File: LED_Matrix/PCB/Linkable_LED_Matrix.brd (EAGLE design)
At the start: 32 x 32 mm, 9 parts

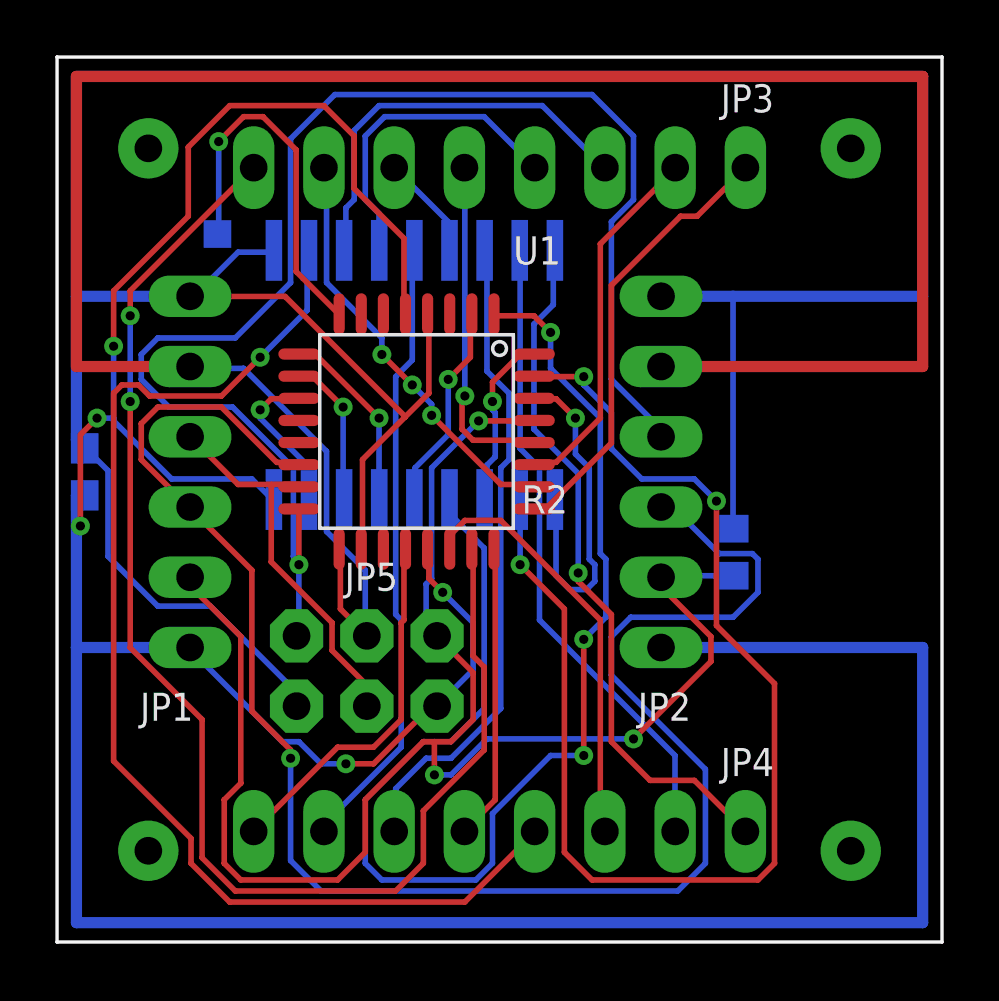
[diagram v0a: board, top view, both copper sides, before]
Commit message: led - matrix - new mounting holes, rerouted...
Added new mounting hole strategy - holes are 0.125" unplated, and can mount
with m2.5 screws, or plastic pressfit standoffs.

Silikscreen cleaned up - all labels moved away from vias, and placed upright.
Added clear labelling for all parts, and put horizontal lines across the board
showing chaining connectivity.

Put ATTINY's decoupling cap closer to part.

12 mil traces for passthru VCC/GND/SCLK.  All others 8mil.

Removed unused test pad.
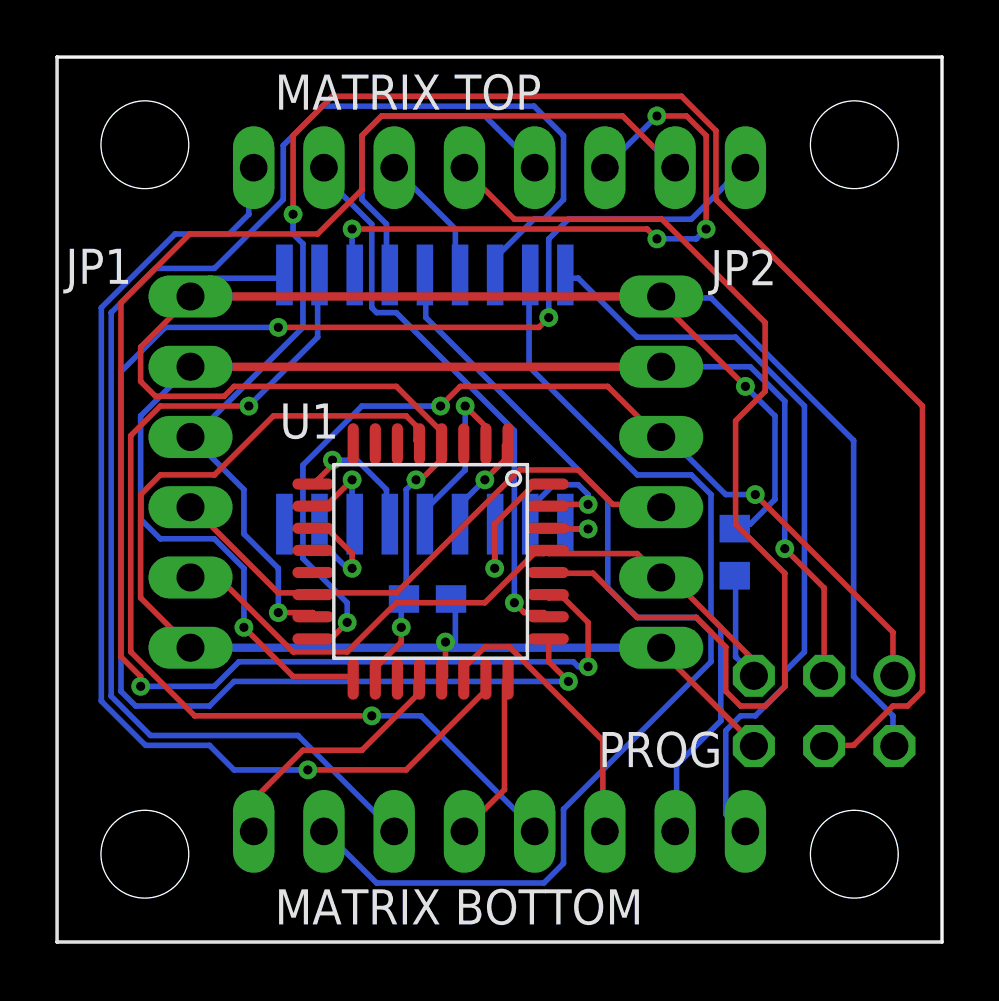
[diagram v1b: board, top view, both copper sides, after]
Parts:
- removed U$1: ATTINY48, ScottSilver:ATTINY48
- removed U$2: ULN2803AFWG, ScottSilver:ULN2803AFWG
- removed U$3: 8X8_LED_MATRIX, ScottSilver:8X8_LED_MATRIX
- removed U$5: 1X1MM_PAD, ScottSilver:1X1MM_PAD
- removed U$6, U$7: DIP1X6MALE, ScottSilver:DIP1X6MALE
- removed U$9: DIP2X3MALE, ScottSilver:DIP2X3MALE
- added JP1, JP2: (no value), raspberrystem:1X06
- added LEDMATRIX: 8X8_LED_MATRIX, raspberrystem:8X8_LED_MATRIX
- added PROG: (no value), raspberrystem:MA03-2
- added U1: ATTINY48, raspberrystem:ATTINY48
- added U2: ULN2803AFWG, raspberrystem:ULN2803AFWG
- moved C1 13.2 mm to (13.4, 12.4), turned to 180 degrees
- moved R1 0.05 mm to (24.5, 14.1)
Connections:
- removed net N$13: U$1.PB7, U$5.P$1
- net COL0: now also U1.PD0, U2.I1; no longer U$1.PD0, U$2.I1
- net COL1: now also U1.PD1, U2.I2; no longer U$1.PD1, U$2.I2
- net COL2: now also U1.PD2, U2.I3; no longer U$1.PD2, U$2.I3
- net COL3: now also U1.PD3, U2.I4; no longer U$1.PD3, U$2.I4
- net COL4: now also U1.PD4, U2.I5; no longer U$1.PD4, U$2.I5
- net COL5: now also U1.PD5, U2.I6; no longer U$1.PD5, U$2.I6
- net COL6: now also U1.PD6, U2.I7; no longer U$1.PD6, U$2.I7
- net COL7: now also U1.PD7, U2.I8; no longer U$1.PD7, U$2.I8
- net CS: now also JP1.4, JP2.4, U1.PB2; no longer U$1.PB2, U$6.3, U$7.3
- net GND: now also JP1.6, JP2.6, PROG.6, U1.AGND, U1.GND; no longer U$1.AGND, U$1.GND, U$2.GND, U$6.1, U$7.1, U$9.GND
- net MISO: now also JP2.3, PROG.1, U1.PB4; no longer U$1.PB4, U$7.4, U$9.MISO
- net MOSI: now also JP1.3, PROG.4, U1.PB3; no longer U$1.PB3, U$6.4, U$9.MOSI
- net N$1: now also LEDMATRIX.COL0, U2.O1; no longer U$2.O1, U$3.COL0
- net N$2: now also LEDMATRIX.COL1, U2.O2; no longer U$2.O2, U$3.COL1
- net N$3: now also LEDMATRIX.COL2, U2.O3; no longer U$2.O3, U$3.COL2
- net N$4: now also LEDMATRIX.COL3, U2.O4; no longer U$2.O4, U$3.COL3
- net N$5: now also LEDMATRIX.COL4, U2.O5; no longer U$2.O5, U$3.COL4
- net N$6: now also LEDMATRIX.COL5, U2.O6; no longer U$2.O6, U$3.COL5
- net N$7: now also LEDMATRIX.COL6, U2.O7; no longer U$2.O7, U$3.COL6
- net N$8: now also LEDMATRIX.COL7, U2.O8; no longer U$2.O8, U$3.COL7
- net RESET: now also JP1.5, JP2.5, PROG.5, U1.PC6; no longer U$1.PC6, U$6.2, U$7.2, U$9.RESET
- net ROW0: now also LEDMATRIX.ROW0, U1.PC7; no longer U$1.PC7, U$3.ROW0
- net ROW1: now also LEDMATRIX.ROW1, U1.PA1; no longer U$1.PA1, U$3.ROW1
- net ROW2: now also LEDMATRIX.ROW2, U1.PC0; no longer U$1.PC0, U$3.ROW2
- net ROW3: now also LEDMATRIX.ROW3, U1.PC1; no longer U$1.PC1, U$3.ROW3
- net ROW4: now also LEDMATRIX.ROW4, U1.PC2; no longer U$1.PC2, U$3.ROW4
- net ROW5: now also LEDMATRIX.ROW5, U1.PC3; no longer U$1.PC3, U$3.ROW5
- net ROW6: now also LEDMATRIX.ROW6, U1.PC4; no longer U$1.PC4, U$3.ROW6
- net ROW7: now also LEDMATRIX.ROW7, U1.PC5; no longer U$1.PC5, U$3.ROW7
- net SCK: now also JP1.2, JP2.2, PROG.3, U1.PB5; no longer U$1.PB5, U$6.5, U$7.5, U$9.SCK
- net VCC: now also JP1.1, JP2.1, PROG.2, U1.AVCC, U1.VCC, U2.COMMON; no longer U$1.AVCC, U$1.VCC, U$2.COMMON, U$6.6, U$7.6, U$9.5V
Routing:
- net GND: track 125.5 -> 43.7 mm, vias 5 -> 1
- net MOSI: track 14.2 -> 66.0 mm, vias 0 -> 2
- net ROW6: track 13.3 -> 59.0 mm, vias 0 -> 2
- net COL3: track 45.9 -> 3.66 mm, vias 3 -> 1
- net ROW4: track 16.1 -> 57.4 mm, vias 0 -> 3
- net CS: track 61.9 -> 20.7 mm, vias 1 -> 0
- net COL1: track 45.0 -> 5.09 mm, vias 3 -> 1
- net VCC: track 110.5 -> 78.5 mm, vias 0 -> 3
- net SCK: track 82.2 -> 50.1 mm, vias 0 -> 2
- net N$3: track 23.6 -> 53.5 mm
- net RESET: track 57.8 -> 29.1 mm, vias 3 -> 0
- net ROW7: track 12.3 -> 39.3 mm, vias 1 -> 0
- net MISO: track 53.3 -> 35.6 mm, vias 1 -> 3
- net N$5: track 22.6 -> 38.7 mm
- net N$13: track 13.6 -> 0.00 mm, vias 1 -> 0
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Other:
- outline, holes or cut-outs redrawn
- board text added: "DOUT"
- board text added: "MATRIX BOTTOM"
- board text added: "MATRIX TOP"
- board text removed: "D_O"
- board text removed: "JP1"
- board text removed: "JP2"
- board text removed: "JP3"
- board text removed: "JP4"
- board text removed: "JP5"
- board text removed: "R1"
- board text removed: "R2"
- board text removed: "U1"
- board text removed: "U2"

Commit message: cleanup to pass error checks
Stop mask fails checks for silkscreen written on top of copper, but OshPark
automatically trims that so I've approved it all.  It would be a pain to trim
it all, so I won't (unless we need to later).
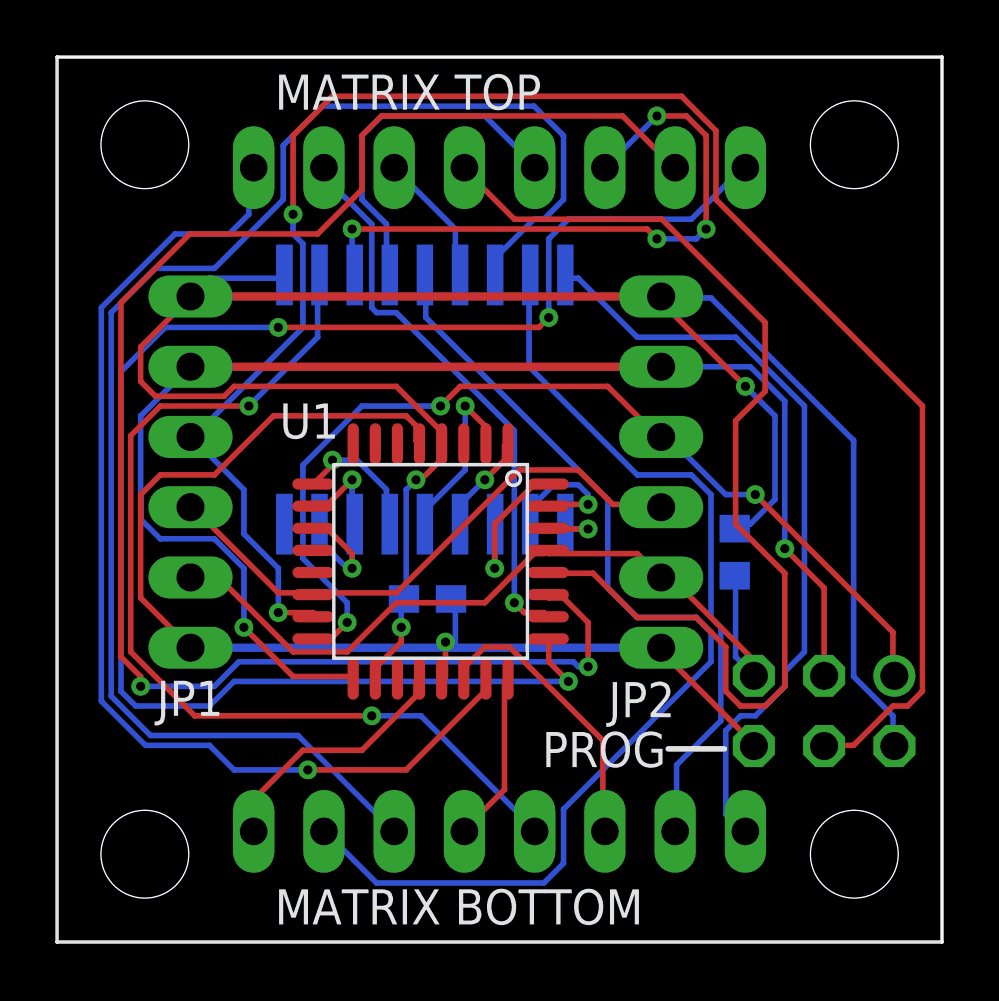
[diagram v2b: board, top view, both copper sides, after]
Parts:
- JP1, JP2, PROG: value (none) -> NONE
- R1: value (none) -> 10k
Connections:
- net GND: now also U2.GND
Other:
- board text added: "CLK"
- board text added: "IN"
- board text added: "OUT"
- board text removed: "DOUT"
- board text removed: "SCK"
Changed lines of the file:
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@@
 <wire x1="32" y1="32" x2="0" y2="32" width="0" layer="20"/>
 <text x="31.496" y="22.86" size="1.27" layer="22" font="vector" rot="MR0">VCC</text>
-<text x="31.496" y="20.32" size="1.27" layer="22" font="vector" rot="MR0">SCK</text>
-<text x="31.496" y="17.78" size="1.27" layer="22" font="vector" rot="MR0">DOUT</text>
+<text x="31.496" y="20.32" size="1.27" layer="22" font="vector" rot="MR0">CLK</text>
+<text x="31.496" y="17.78" size="1.27" layer="22" font="vector" rot="MR0">OUT</text>
 <text x="31.496" y="15.24" size="1.27" layer="22" font="vector" rot="MR0">CS</text>
 <text x="31.496" y="12.7" size="1.27" layer="22" font="vector" rot="MR0">RST</text>
@@
 <wire x1="27.94" y1="13.208" x2="0.381" y2="13.208" width="0.2032" layer="22"/>
 <wire x1="28.829" y1="15.748" x2="0.381" y2="15.748" width="0.2032" layer="22"/>
-<wire x1="26.797" y1="18.288" x2="0.381" y2="18.288" width="0.2032" layer="22"/>
+<wire x1="26.797" y1="18.288" x2="2.286" y2="18.288" width="0.2032" layer="22"/>
 <wire x1="27.686" y1="20.828" x2="0.381" y2="20.828" width="0.2032" layer="22"/>
 <wire x1="27.686" y1="23.368" x2="0.381" y2="23.368" width="0.2032" layer="22"/>
 <rectangle x1="28.194" y1="10.16" x2="31.877" y2="24.257" layer="43"/>
-<rectangle x1="26.797" y1="17.399" x2="32.004" y2="19.304" layer="43"/>
 <wire x1="25.781" y1="10.668" x2="26.289" y2="11.176" width="0.2032" layer="22"/>
 <wire x1="26.289" y1="11.176" x2="27.686" y2="11.176" width="0.2032" layer="22"/>
 <text x="7.874" y="30.099" size="1.27" layer="21" font="vector">MATRIX TOP</text>
 <text x="7.874" y="0.635" size="1.27" layer="21" font="vector">MATRIX BOTTOM</text>
+<wire x1="22.098" y1="6.985" x2="24.13" y2="6.985" width="0.2032" layer="21"/>
+<text x="2.032" y="17.78" size="1.27" layer="22" font="vector" rot="MR0">IN</text>
+<rectangle x1="0" y1="17.399" x2="2.413" y2="19.431" layer="43"/>
 </plain>
 <attributes>
@@
 </element>
 <element name="LEDMATRIX" library="raspberrystem" package="8X8_LED_MATRIX" value="8X8_LED_MATRIX" x="16" y="16"/>
-<element name="R1" library="resistor" package="R0603" value="" x="24.5048" y="14.096" smashed="yes" rot="MR270">
+<element name="R1" library="resistor" package="R0603" value="10k" x="24.5048" y="14.096" smashed="yes" rot="MR270">
 <attribute name="NAME" x="23.3618" y="12.445" size="1.27" layer="26" rot="MR180"/>
-<attribute name="VALUE" x="26.5368" y="14.985" size="1.27" layer="28" rot="MR270"/>
 </element>
 <element name="C1" library="resistor" package="C0603" value="1uF" x="13.3952" y="12.4026" smashed="yes" rot="MR180">
 <attribute name="NAME" x="14.2842" y="11.6406" size="1.27" layer="26" rot="MR180"/>
 </element>
-<element name="PROG" library="raspberrystem" package="MA03-2" value="" x="27.7368" y="8.3566" smashed="yes" rot="R180">
+<element name="PROG" library="raspberrystem" package="MA03-2" value="NONE" x="27.7368" y="8.3566" smashed="yes" rot="R180">
 <attribute name="OC_NEWARK" value="unknown" x="27.7368" y="8.3566" size="1.778" layer="27" rot="R180" display="off"/>
 <attribute name="MPN" value="" x="27.7368" y="8.3566" size="1.778" layer="27" rot="R180" display="off"/>
 <attribute name="MF" value="" x="27.7368" y="8.3566" size="1.778" layer="27" rot="R180" display="off"/>
 <attribute name="OC_FARNELL" value="unknown" x="27.7368" y="8.3566" size="1.778" layer="27" rot="R180" display="off"/>
-<attribute name="NAME" x="24.0538" y="7.5946" size="1.27" layer="25" ratio="10" rot="R180"/>
+<attribute name="NAME" x="22.0218" y="7.5946" size="1.27" layer="25" ratio="10" rot="R180"/>
 </element>
-<element name="JP1" library="raspberrystem" package="1X06" value="" x="4.826" y="16.9926" smashed="yes" rot="R270">
-<attribute name="NAME" x="0.3048" y="23.7998" size="1.27" layer="25" ratio="10"/>
-<attribute name="VALUE" x="1.651" y="24.6126" size="1.27" layer="27" rot="R270"/>
+<element name="JP1" library="raspberrystem" package="1X06" value="NONE" x="4.826" y="16.9926" smashed="yes" rot="R270">
+<attribute name="NAME" x="3.6068" y="8.1788" size="1.27" layer="25" ratio="10"/>
 </element>
-<element name="JP2" library="raspberrystem" package="1X06" value="" x="21.844" y="16.9926" smashed="yes" rot="R270">
-<attribute name="NAME" x="23.622" y="23.749" size="1.27" layer="25" ratio="10"/>
-<attribute name="VALUE" x="18.669" y="24.6126" size="1.27" layer="27" rot="R270"/>
+<element name="JP2" library="raspberrystem" package="1X06" value="NONE" x="21.844" y="16.9926" smashed="yes" rot="R270">
+<attribute name="NAME" x="19.939" y="8.128" size="1.27" layer="25" ratio="10"/>
 </element>
 </elements>
@@
 <wire x1="12.9794" y1="18.1356" x2="13.108" y2="18.011" width="0.2032" layer="1"/>
 <via x="14.0462" y="10.8458" extent="1-16" drill="0.3302"/>
+<contactref element="U2" pad="GND"/>
+<wire x1="5.6896" y1="16.891" x2="8.221" y2="15.111" width="0" layer="19" extent="1-16"/>
 </signal>
 <signal name="SCK">
@@
 </signal>
 </signals>
+<errors>
+</errors>
 </board>
 </drawing>
